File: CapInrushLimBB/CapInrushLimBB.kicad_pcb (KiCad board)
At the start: 2 copper layers, 56.5 x 34.9 mm, 29 parts, among them J1 Screw_Terminal_01x02, J2 Screw_Terminal_01x02, K1 G5LE-1A, Q1 MPSA42, Q2 IRF9540N, Q3 MPSA42, Q4 Q_PMOS_GDSD

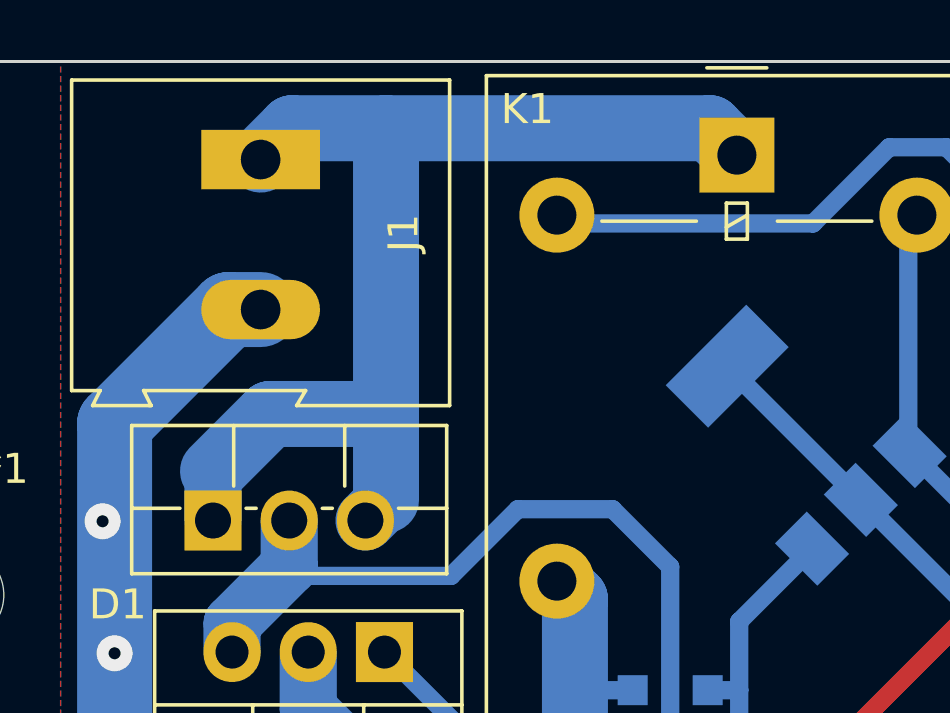
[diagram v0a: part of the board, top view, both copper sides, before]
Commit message: Tweaked track widths around high current tracks.
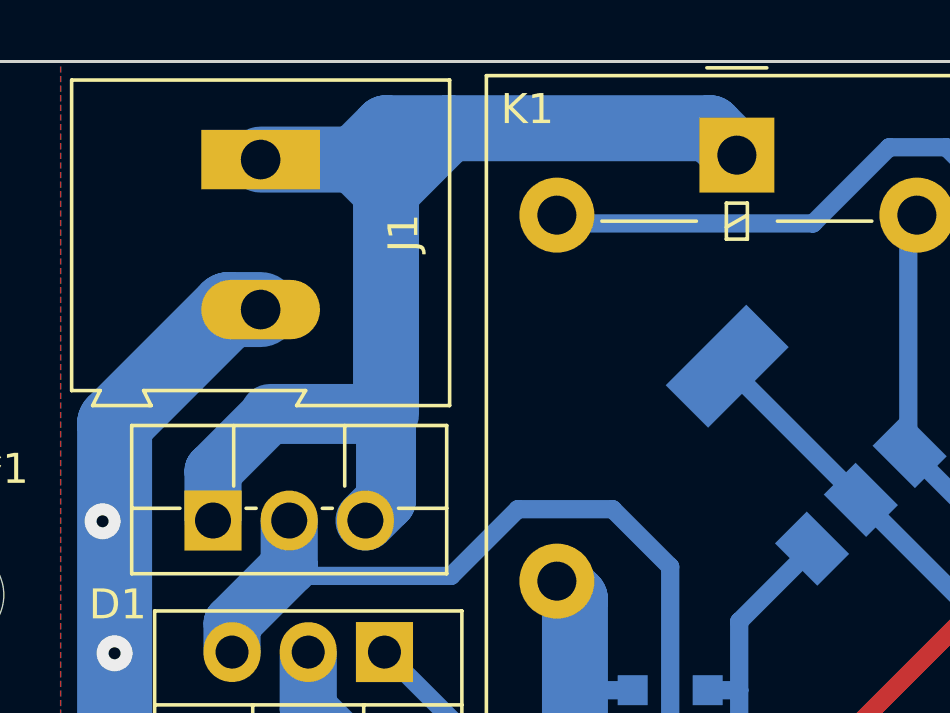
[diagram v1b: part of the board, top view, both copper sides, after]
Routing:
- net /RL_Input: track 38.2 -> 40.6 mm
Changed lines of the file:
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@@
   (segment (start 252.4125 147.955) (end 252.4125 147.6375) (width 0.6096) (layer "B.Cu") (net 4))
   (segment (start 249.965 145.19) (end 249.965 144.4625) (width 0.6096) (layer "B.Cu") (net 4))
-  (segment (start 225.16 127.635) (end 235.9575 127.635) (width 2.2) (layer "B.Cu") (net 5))
-  (segment (start 235.9575 127.635) (end 236.855 128.5325) (width 2.2) (layer "B.Cu") (net 5))
-  (segment (start 222.025 127.635) (end 225.16 127.635) (width 2.2) (layer "B.Cu") (net 5))
-  (segment (start 220.98 128.68) (end 222.025 127.635) (width 2.2) (layer "B.Cu") (net 5))
-  (segment (start 221.2975 137.16) (end 225.16 137.16) (width 2.2) (layer "B.Cu") (net 5))
-  (segment (start 225.16 140.025) (end 225.16 137.16) (width 2.2) (layer "B.Cu") (net 5))
-  (segment (start 225.16 137.16) (end 225.16 127.635) (width 2.2) (layer "B.Cu") (net 5))
-  (segment (start 219.3925 139.065) (end 221.2975 137.16) (width 2.2) (layer "B.Cu") (net 5))
+  (segment (start 227.25 127.635) (end 225.16 127.635) (width 2.2) (layer "B.Cu") (net 5))
+  (segment (start 224.115 128.68) (end 225.16 127.635) (width 2.2) (layer "B.Cu") (net 5))
+  (segment (start 225.16 129.725) (end 224.115 128.68) (width 2.2) (layer "B.Cu") (net 5))
+  (segment (start 224.115 128.68) (end 220.98 128.68) (width 2.2) (layer "B.Cu") (net 5))
+  (segment (start 221.2975 137.16) (end 225.16 137.16) (width 2) (layer "B.Cu") (net 5))
+  (segment (start 225.16 140.025) (end 225.16 137.16) (width 2) (layer "B.Cu") (net 5))
+  (segment (start 225.16 129.725) (end 227.25 127.635) (width 2.2) (layer "B.Cu") (net 5))
+  (segment (start 219.3925 139.065) (end 221.2975 137.16) (width 1.905) (layer "B.Cu") (net 5))
   (segment (start 225.16 140.025) (end 224.4725 140.7125) (width 2) (layer "B.Cu") (net 5))
+  (segment (start 235.9575 127.635) (end 227.25 127.635) (width 2.2) (layer "B.Cu") (net 5))
+  (segment (start 225.16 129.725) (end 225.16 137.16) (width 2.2) (layer "B.Cu") (net 5))
+  (segment (start 236.855 128.5325) (end 235.9575 127.635) (width 2.2) (layer "B.Cu") (net 5))
   (segment (start 219.3925 140.7125) (end 219.3925 139.065) (width 1.905) (layer "B.Cu") (net 5))
   (segment (start 253.6825 140.0175) (end 252.574315 138.909315) (width 0.6096) (layer "B.Cu") (net 6))

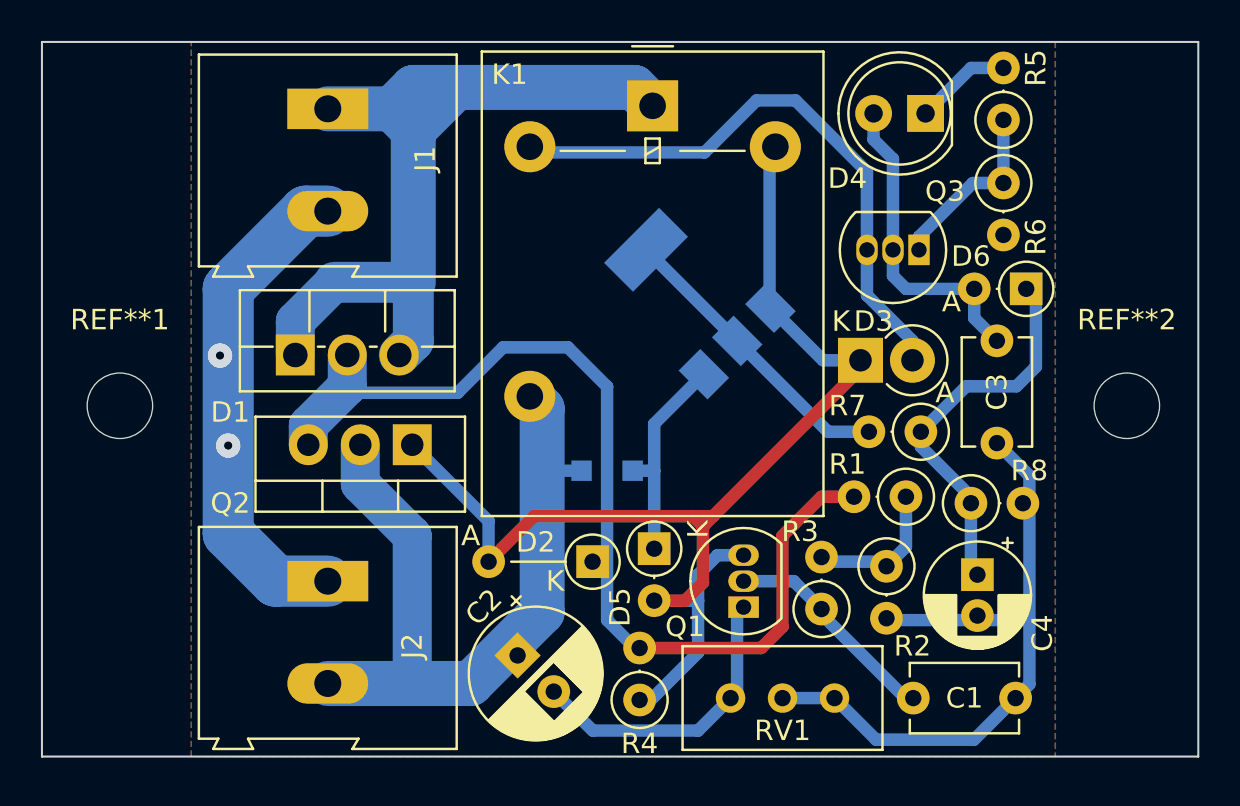
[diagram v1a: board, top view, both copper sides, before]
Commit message: Tweaked track position to equalise track clearance.
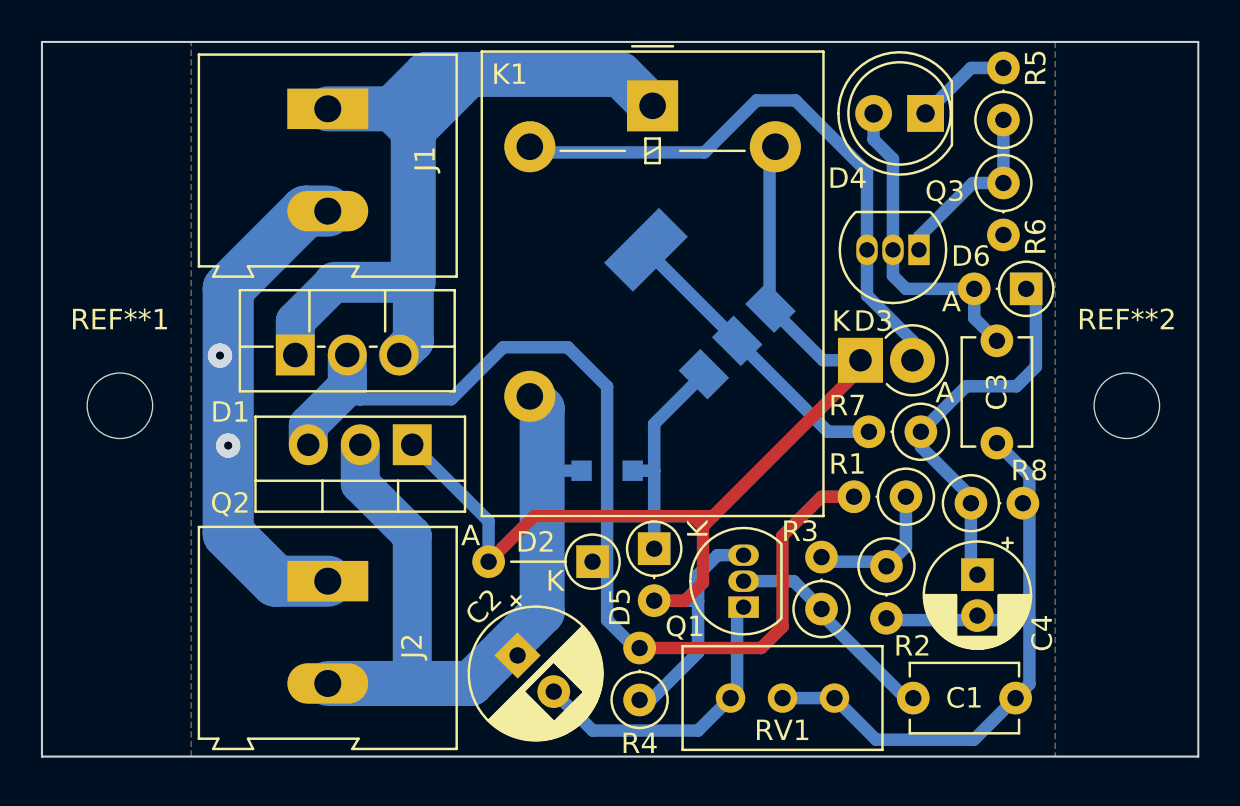
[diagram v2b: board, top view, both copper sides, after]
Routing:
- net /PolProtect: track 48.8 -> 52.2 mm
- net /RL_Input: track 40.6 -> 42.0 mm
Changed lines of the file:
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@@
   (segment (start 252.4125 147.955) (end 252.4125 147.6375) (width 0.6096) (layer "B.Cu") (net 4))
   (segment (start 249.965 145.19) (end 249.965 144.4625) (width 0.6096) (layer "B.Cu") (net 4))
-  (segment (start 227.25 127.635) (end 225.16 127.635) (width 2.2) (layer "B.Cu") (net 5))
-  (segment (start 224.115 128.68) (end 225.16 127.635) (width 2.2) (layer "B.Cu") (net 5))
+  (segment (start 224.115 128.68) (end 225.795 127) (width 2.2) (layer "B.Cu") (net 5))
+  (segment (start 225.16 129.725) (end 227.885 127) (width 2.2) (layer "B.Cu") (net 5))
+  (segment (start 235.2675 127) (end 236.8 128.5325) (width 2.2) (layer "B.Cu") (net 5))
+  (segment (start 236.8 128.5325) (end 236.855 128.5325) (width 2.2) (layer "B.Cu") (net 5))
   (segment (start 225.16 129.725) (end 224.115 128.68) (width 2.2) (layer "B.Cu") (net 5))
   (segment (start 224.115 128.68) (end 220.98 128.68) (width 2.2) (layer "B.Cu") (net 5))
   (segment (start 221.2975 137.16) (end 225.16 137.16) (width 2) (layer "B.Cu") (net 5))
   (segment (start 225.16 140.025) (end 225.16 137.16) (width 2) (layer "B.Cu") (net 5))
-  (segment (start 225.16 129.725) (end 227.25 127.635) (width 2.2) (layer "B.Cu") (net 5))
+  (segment (start 225.795 127) (end 227.885 127) (width 2.2) (layer "B.Cu") (net 5))
+  (segment (start 227.885 127) (end 235.2675 127) (width 2.2) (layer "B.Cu") (net 5))
   (segment (start 219.3925 139.065) (end 221.2975 137.16) (width 1.905) (layer "B.Cu") (net 5))
   (segment (start 225.16 140.025) (end 224.4725 140.7125) (width 2) (layer "B.Cu") (net 5))
-  (segment (start 235.9575 127.635) (end 227.25 127.635) (width 2.2) (layer "B.Cu") (net 5))
   (segment (start 225.16 129.725) (end 225.16 137.16) (width 2.2) (layer "B.Cu") (net 5))
-  (segment (start 236.855 128.5325) (end 235.9575 127.635) (width 2.2) (layer "B.Cu") (net 5))
   (segment (start 219.3925 140.7125) (end 219.3925 139.065) (width 1.905) (layer "B.Cu") (net 5))
   (segment (start 253.6825 140.0175) (end 252.574315 138.909315) (width 0.6096) (layer "B.Cu") (net 6))
@@
   (segment (start 246.6975 147.6375) (end 245.11 147.6375) (width 0.6096) (layer "F.Cu") (net 14))
   (segment (start 243.205 149.5425) (end 243.205 153.9875) (width 0.6096) (layer "F.Cu") (net 14))
-  (segment (start 222.420474 142.5575) (end 227.33 142.5575) (width 0.6096) (layer "B.Cu") (net 14))
-  (segment (start 227.33 142.5575) (end 229.5525 140.335) (width 0.6096) (layer "B.Cu") (net 14))
+  (segment (start 234.6325 142.253878) (end 232.713622 140.335) (width 0.6096) (layer "B.Cu") (net 14))
+  (segment (start 222.5675 142.875) (end 222.5675 141.3475) (width 0.6096) (layer "B.Cu") (net 14))
   (segment (start 221.9325 140.7125) (end 221.9325 142.24) (width 1.905) (layer "B.Cu") (net 14))
-  (segment (start 232.713622 140.335) (end 234.6325 142.253878) (width 0.6096) (layer "B.Cu") (net 14))
+  (segment (start 232.713622 140.335) (end 229.5525 140.335) (width 0.6096) (layer "B.Cu") (net 14))
   (segment (start 220.0275 144.145) (end 220.0275 145.0975) (width 1.905) (layer "B.Cu") (net 14))
-  (segment (start 234.6325 142.253878) (end 234.6325 153.67) (width 0.6096) (layer "B.Cu") (net 14))
-  (segment (start 235.995 155.0325) (end 236.22 155.0325) (width 0.6096) (layer "B.Cu") (net 14))
-  (segment (start 234.6325 153.67) (end 235.995 155.0325) (width 0.6096) (layer "B.Cu") (net 14))
+  (segment (start 235.995 155.0325) (end 234.6325 153.67) (width 0.6096) (layer "B.Cu") (net 14))
+  (segment (start 229.5525 140.335) (end 227.0125 142.875) (width 0.6096) (layer "B.Cu") (net 14))
   (segment (start 221.9325 142.24) (end 220.0275 144.145) (width 1.905) (layer "B.Cu") (net 14))
-  (segment (start 229.5525 140.335) (end 232.713622 140.335) (width 0.6096) (layer "B.Cu") (net 14))
+  (segment (start 222.5675 142.875) (end 220.6625 142.875) (width 0.6096) (layer "B.Cu") (net 14))
+  (segment (start 234.6325 153.67) (end 234.6325 142.253878) (width 0.6096) (layer "B.Cu") (net 14))
+  (segment (start 236.22 155.0325) (end 235.995 155.0325) (width 0.6096) (layer "B.Cu") (net 14))
+  (segment (start 227.0125 142.875) (end 222.5675 142.875) (width 0.6096) (layer "B.Cu") (net 14))
   (zone (net 13) (net_name "/Gnd") (layers F&B.Cu) (hatch edge 0.508)
     (connect_pads (clearance 0.508))

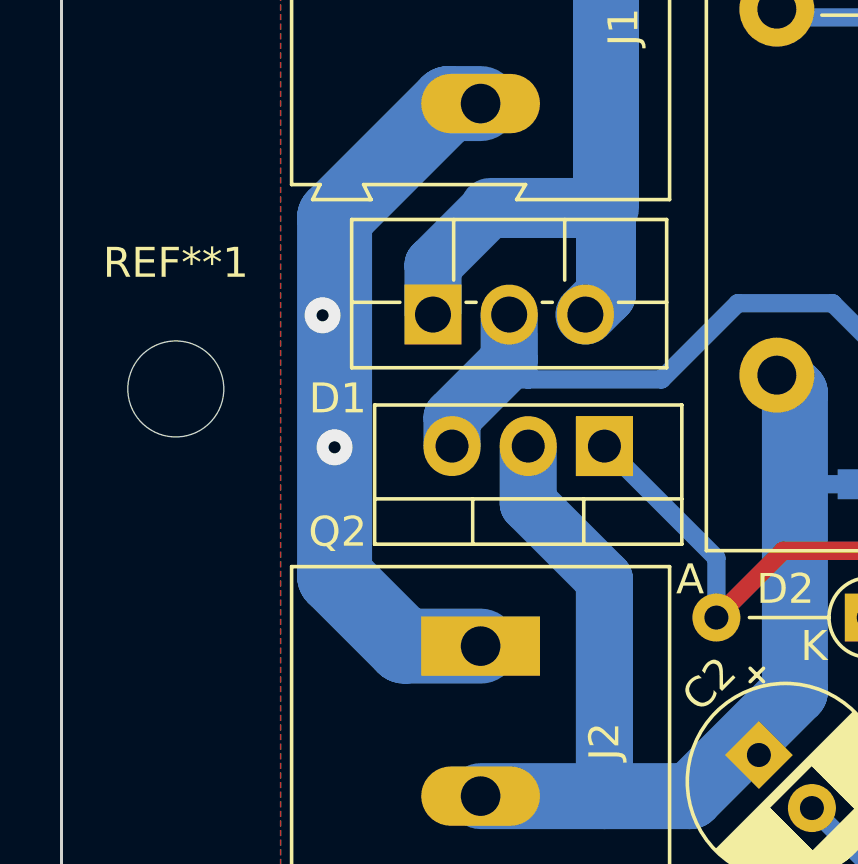
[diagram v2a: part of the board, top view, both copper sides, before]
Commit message: Added artwork and tweaked Gnd track in unrounded PCB
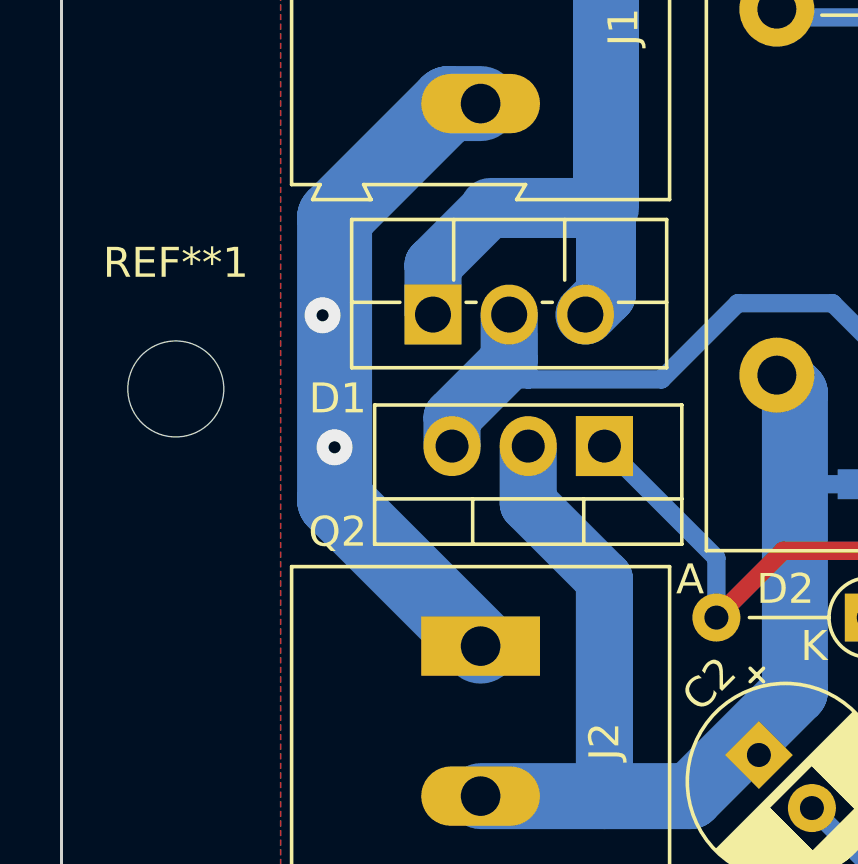
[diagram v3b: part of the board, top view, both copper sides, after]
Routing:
- net /Gnd: track 62.3 -> 60.8 mm
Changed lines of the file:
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@@
   (segment (start 255.27 146.605) (end 253.6825 145.0175) (width 0.6096) (layer "B.Cu") (net 13))
   (segment (start 247.7775 159.5125) (end 245.745 157.48) (width 0.6096) (layer "B.Cu") (net 13))
-  (segment (start 218.44 151.765) (end 216.1125 149.4375) (width 2.5) (layer "B.Cu") (net 13))
-  (segment (start 219.91 133.68) (end 216.1125 137.4775) (width 2.5) (layer "B.Cu") (net 13))
   (segment (start 255.27 146.605) (end 255.27 147.6375) (width 0.6096) (layer "B.Cu") (net 13))
   (segment (start 254.595 157.48) (end 255.27 156.805) (width 0.6096) (layer "B.Cu") (net 13))
   (segment (start 243.205 157.48) (end 245.745 157.48) (width 0.6096) (layer "B.Cu") (net 13))
   (segment (start 254.595 157.48) (end 252.5625 159.5125) (width 0.6096) (layer "B.Cu") (net 13))
-  (segment (start 216.1125 149.4375) (end 216.1125 137.4775) (width 2.5) (layer "B.Cu") (net 13))
   (segment (start 252.9525 153.67) (end 255.27 153.67) (width 0.6096) (layer "B.Cu") (net 13))
-  (segment (start 220.98 133.68) (end 219.91 133.68) (width 2.5) (layer "B.Cu") (net 13))
   (segment (start 255.27 153.67) (end 255.27 148.2725) (width 0.6096) (layer "B.Cu") (net 13))
   (segment (start 255.27 148.2725) (end 254.9525 147.955) (width 0.6096) (layer "B.Cu") (net 13))
   (segment (start 255.27 156.805) (end 255.27 153.67) (width 0.6096) (layer "B.Cu") (net 13))
+  (segment (start 219.91 133.68) (end 216.1125 137.4775) (width 2.5) (layer "B.Cu") (net 13))
   (segment (start 248.3775 153.67) (end 248.285 153.5775) (width 0.6096) (layer "B.Cu") (net 13))
-  (segment (start 220.98 151.765) (end 218.44 151.765) (width 2.5) (layer "B.Cu") (net 13))
+  (segment (start 220.98 133.68) (end 219.91 133.68) (width 2.5) (layer "B.Cu") (net 13))
+  (segment (start 216.1125 137.4775) (end 216.1125 146.8975) (width 2.5) (layer "B.Cu") (net 13))
+  (segment (start 216.1125 146.8975) (end 220.98 151.765) (width 2.5) (layer "B.Cu") (net 13))
   (segment (start 243.205 153.9875) (end 242.16 155.0325) (width 0.6096) (layer "F.Cu") (net 14))
   (segment (start 242.16 155.0325) (end 236.22 155.0325) (width 0.6096) (layer "F.Cu") (net 14))
